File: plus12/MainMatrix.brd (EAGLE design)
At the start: 114.3 x 73.7 mm, 41 parts, among them SW1 RSTSWSMD, SW2 TRANSFERPADDY

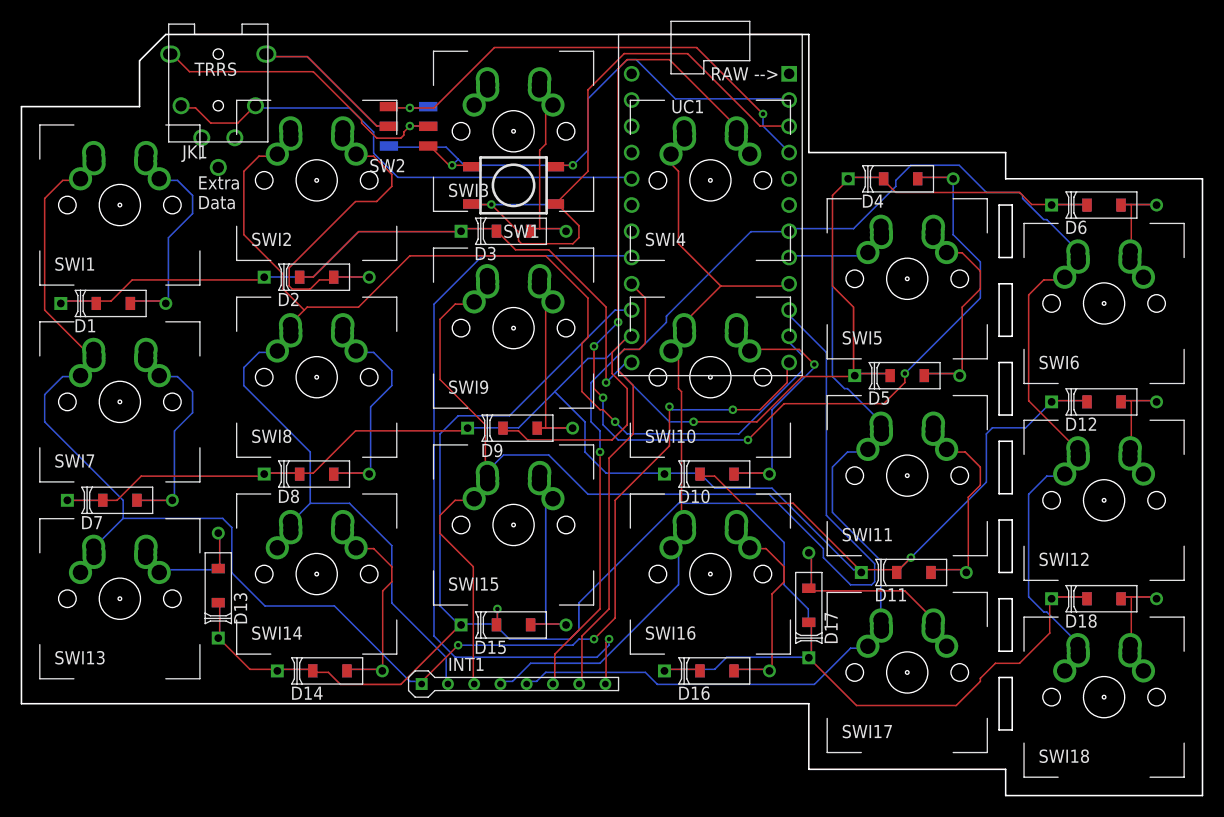
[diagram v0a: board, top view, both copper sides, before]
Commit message: Adding straight thumbs, using Othermill DRCs
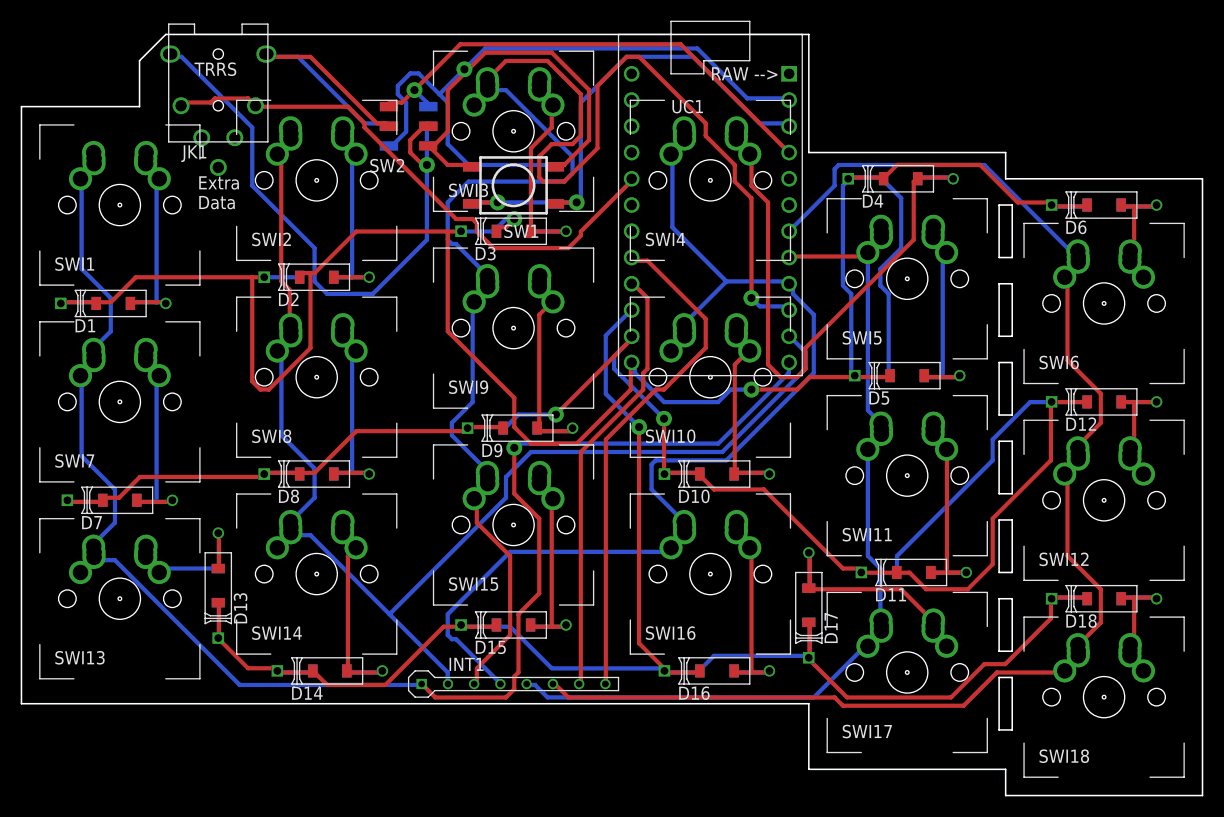
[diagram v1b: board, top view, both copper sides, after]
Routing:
- net N$5: track 113.6 -> 55.7 mm, vias 5 -> 0
- net N$35: track 56.2 -> 104.5 mm, vias 2 -> 1
- net N$20: track 180.9 -> 218.2 mm
- net N$22: track 198.7 -> 164.3 mm
- net N$25: track 128.7 -> 159.7 mm, vias 0 -> 1
- net N$30: track 31.4 -> 59.3 mm
- net N$33: track 76.6 -> 49.4 mm, vias 1 -> 0
- net N$24: track 152.0 -> 126.4 mm, vias 1 -> 0
- net N$26: track 82.5 -> 107.9 mm
- net N$3: track 32.2 -> 19.0 mm
- net N$34: track 61.3 -> 49.9 mm, vias 1 -> 2
- net N$21: track 187.7 -> 178.2 mm, vias 1 -> 2
- net N$27: track 148.0 -> 139.1 mm, vias 1 -> 0
- net N$11: track 26.4 -> 19.5 mm, vias 1 -> 0
- net N$32: track 49.2 -> 53.9 mm
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
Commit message: Kobe beefing it up
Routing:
- net N$21: track 178.2 -> 228.4 mm, vias 2 -> 0
- net N$32: track 53.9 -> 102.3 mm
- net N$26: track 107.9 -> 76.4 mm
- net N$1: track 90.8 -> 121.8 mm
- net N$29: track 42.1 -> 64.5 mm, vias 0 -> 3
- net N$20: track 218.2 -> 199.4 mm, vias 2 -> 3
- net N$5: track 55.7 -> 39.7 mm
- net N$30: track 59.3 -> 48.5 mm
- net N$35: track 104.5 -> 115.3 mm, vias 1 -> 2
- net N$25: track 159.7 -> 150.1 mm
- net N$33: track 49.4 -> 44.3 mm, vias 0 -> 1
- net N$22: track 164.3 -> 159.6 mm, vias 1 -> 2
- net N$28: track 47.9 -> 51.2 mm, vias 1 -> 3
- net N$23: track 153.1 -> 150.0 mm, vias 1 -> 0
- net N$27: track 139.1 -> 142.1 mm
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
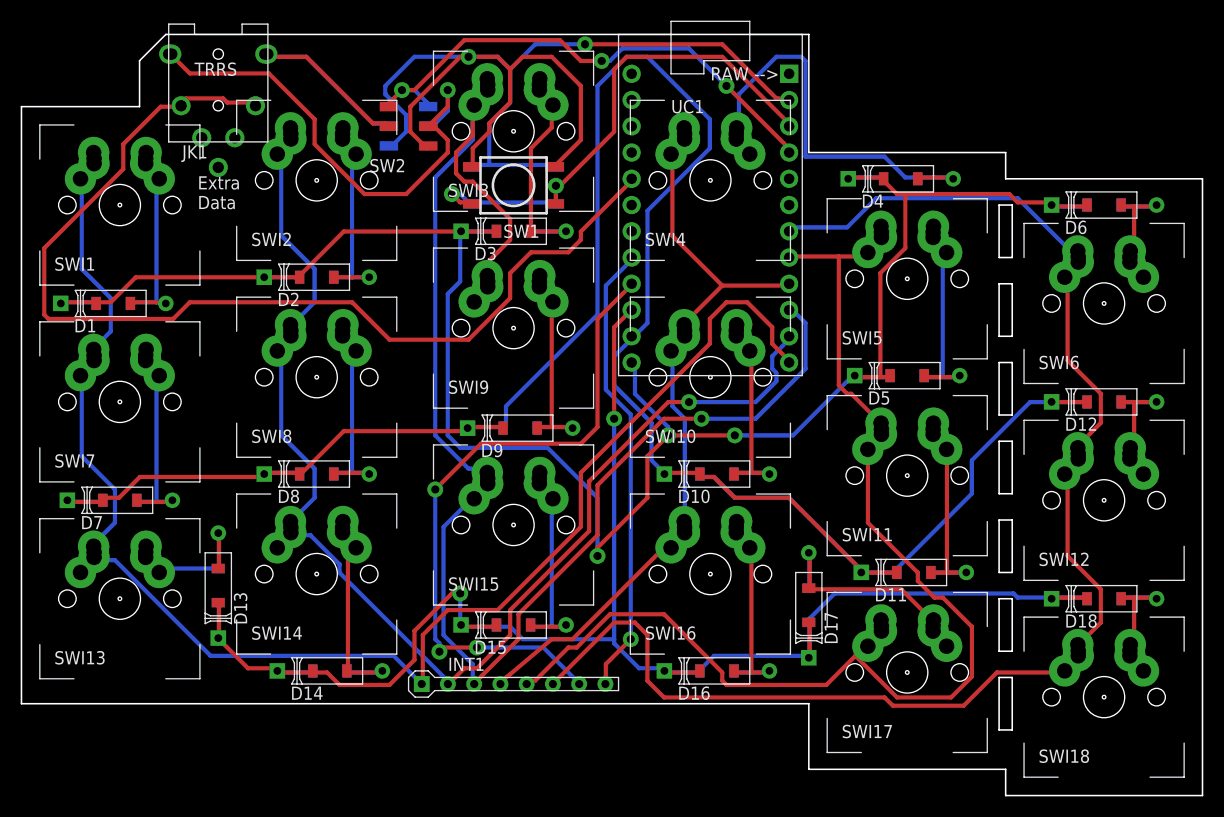
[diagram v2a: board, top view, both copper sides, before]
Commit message: Updating library pad sizes
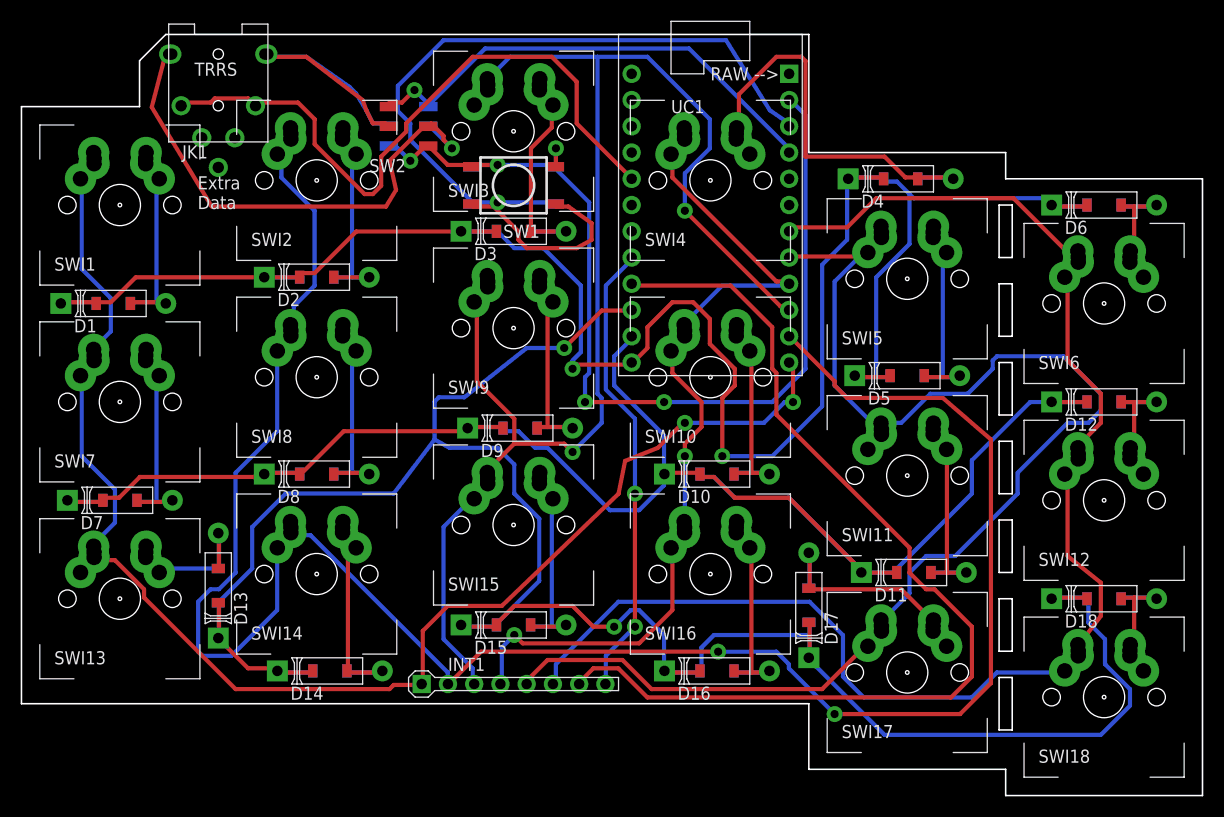
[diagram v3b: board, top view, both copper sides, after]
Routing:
- net N$24: track 127.4 -> 208.5 mm, vias 1 -> 2
- net N$22: track 159.6 -> 216.0 mm
- net N$21: track 228.4 -> 173.6 mm
- net N$32: track 102.3 -> 64.5 mm
- net N$34: track 50.8 -> 87.1 mm, vias 2 -> 1
- net N$29: track 64.5 -> 98.3 mm, vias 3 -> 0
- net N$1: track 121.8 -> 139.3 mm
- net N$35: track 115.3 -> 98.4 mm, vias 2 -> 5
- net N$26: track 76.4 -> 89.6 mm, vias 0 -> 2
- net N$23: track 150.0 -> 144.5 mm, vias 0 -> 2
- net N$27: track 142.1 -> 145.6 mm
- net N$28: track 51.2 -> 47.7 mm, vias 3 -> 1
- net N$30: track 48.5 -> 50.7 mm
- net N$25: track 150.1 -> 148.0 mm, vias 1 -> 2
- net N$31: track 29.8 -> 30.7 mm
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
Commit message: Updates, BEFORE C5/6 Move
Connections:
- net N$32: now also UC1.P$6; no longer UC1.P$5
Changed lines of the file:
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@@
 </layers>
 <board>
+<fusionsync huburn="a.cGVyc29uYWw6dWUyOWMyYTg0" projecturn="a.cGVyc29uYWw6dWUyOWMyYTg0IzIwMTYwODI0NDAzNzc1NzY" f3durn="urn:adsk.wipprod:dm.lineage:ImncLT7-SniIIVQvyqa4_g" pcbguid="19f6bae0-fb57-4887-879c-613a1d8bf549" lastpulledtime="" lastsyncedchangeguid="b71132fa-e0e7-4efc-7cac-1412e2e1ab23"/>
 <plain>
 <wire x1="41.275" y1="111.125" x2="52.705" y2="111.125" width="0.1524" layer="20"/>
@@
 </signal>
 <signal name="N$32">
-<contactref element="UC1" pad="P$5"/>
 <contactref element="JK1" pad="2T"/>
 <contactref element="JK1" pad="2B"/>
@@
 <wire x1="68.037815625" y1="111.517603125" x2="69.648178125" y2="109.907240625" width="0.4064" layer="1"/>
 <wire x1="64.011909375" y1="111.517603125" x2="68.037815625" y2="111.517603125" width="0.4064" layer="1"/>
-<wire x1="100.245065625" y1="104.270971875" x2="100.33" y2="104.14" width="0.4064" layer="1"/>
 <wire x1="64.011909375" y1="111.517603125" x2="63.925" y2="111.21" width="0.4064" layer="1"/>
 <wire x1="59.5834125" y1="111.517603125" x2="56.765278125" y2="111.517603125" width="0.4064" layer="1"/>
@@
 <wire x1="56.765278125" y1="111.517603125" x2="56.725" y2="111.21" width="0.4064" layer="1"/>
 <wire x1="63.60931875" y1="111.517603125" x2="63.925" y2="111.21" width="0.4064" layer="1"/>
+<contactref element="UC1" pad="P$6"/>
+<wire x1="100.245065625" y1="104.270971875" x2="100.33" y2="101.6" width="0" layer="19" extent="1-1"/>
 </signal>
 <signal name="N$29">
@@
 </note>
 <note version="8.3" severity="warning">
+Since Version 8.3, EAGLE supports Fusion synchronisation.
+This feature will not be available in this version and saving
+the document will break the link to the Fusion PCB feature.
+</note>
+<note version="8.3" severity="warning">
